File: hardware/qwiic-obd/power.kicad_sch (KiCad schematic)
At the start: 34 parts, among them Q501 DMG2301L, Q502 DMG2301L, Q503 MMBT3906, Q504 DMG2301L, U501 AP63203WU, U502 XC9142B50CMR-G

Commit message: Added initial layout (parts dump)
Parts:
- C508, C509, C512, C513, C514: footprint (none) -> Capacitor_SMD:C_0805_2012Metric_Pad1.18x1.45mm_HandSolder
- L501, L502: footprint (none) -> Inductor_SMD:L_0603_1608Metric_Pad1.05x0.95mm_HandSolder
- U502: footprint SC_50CMR-G_TOR -> UltraLibrarian:XC9142B50CMR-G
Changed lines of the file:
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@@
     (property "Reference" "L502" (id 0) (at 77.47 171.45 90))
     (property "Value" "4.7uH > 1A" (id 1) (at 77.47 173.99 90))
-    (property "Footprint" "" (id 2) (at 77.47 177.8 0)
+    (property "Footprint" "Inductor_SMD:L_0603_1608Metric_Pad1.05x0.95mm_HandSolder" (id 2) (at 77.47 177.8 0)
       (effects (font (size 1.27 1.27)) hide)
     )
@@
     (property "Reference" "L501" (id 0) (at 111.76 102.87 90))
     (property "Value" "3.9uH > 3A" (id 1) (at 111.76 105.41 90))
-    (property "Footprint" "" (id 2) (at 111.76 109.22 0)
+    (property "Footprint" "Inductor_SMD:L_0603_1608Metric_Pad1.05x0.95mm_HandSolder" (id 2) (at 111.76 109.22 0)
       (effects (font (size 1.27 1.27)) hide)
     )
@@
       (effects (font (size 1.27 1.27)) (justify right))
     )
-    (property "Footprint" "" (id 2) (at 115.2652 166.37 0)
+    (property "Footprint" "Capacitor_SMD:C_0805_2012Metric_Pad1.18x1.45mm_HandSolder" (id 2) (at 115.2652 166.37 0)
       (effects (font (size 1.27 1.27)) hide)
     )
@@
       (effects (font (size 1.524 1.524)))
     )
-    (property "Footprint" "SC_50CMR-G_TOR" (id 2) (at 77.47 150.114 0)
+    (property "Footprint" "UltraLibrarian:XC9142B50CMR-G" (id 2) (at 77.47 150.114 0)
       (effects (font (size 1.524 1.524)) hide)
     )
@@
       (effects (font (size 1.27 1.27)) (justify left))
     )
-    (property "Footprint" "" (id 2) (at 60.6552 128.27 0)
+    (property "Footprint" "Capacitor_SMD:C_0805_2012Metric_Pad1.18x1.45mm_HandSolder" (id 2) (at 60.6552 128.27 0)
       (effects (font (size 1.27 1.27)) hide)
     )
@@
       (effects (font (size 1.27 1.27)) (justify left))
     )
-    (property "Footprint" "" (id 2) (at 126.6952 118.11 0)
+    (property "Footprint" "Capacitor_SMD:C_0805_2012Metric_Pad1.18x1.45mm_HandSolder" (id 2) (at 126.6952 118.11 0)
       (effects (font (size 1.27 1.27)) hide)
     )
@@
       (effects (font (size 1.27 1.27)) (justify left))
     )
-    (property "Footprint" "" (id 2) (at 144.4752 118.11 0)
+    (property "Footprint" "Capacitor_SMD:C_0805_2012Metric_Pad1.18x1.45mm_HandSolder" (id 2) (at 144.4752 118.11 0)
       (effects (font (size 1.27 1.27)) hide)
     )
@@
       (effects (font (size 1.27 1.27)) (justify right))
     )
-    (property "Footprint" "" (id 2) (at 46.6852 163.83 0)
-      (effects (font (size 1.27 1.27)) hide)
-    )
+    (property "Footprint" "Capacitor_SMD:C_0805_2012Metric_Pad1.18x1.45mm_HandSolder" (id 2) (at 46.6852 163.83 0)
+      (effects (font (size 1.27 1.27)) hide)
+    )

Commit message: OK, layout v1 complete
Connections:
- net +3V3: no longer C514.2, C515.1, C516.1, R506.1, U502.4 (VOUT)
- new net +5V: C514.2, C515.1, C516.1, R506.1, U502.4 (VOUT)
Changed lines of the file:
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@@
   (junction (at 97.79 49.53) (diameter 0) (color 0 0 0 0)
   )
+  (junction (at 156.21 161.3913) (diameter 0) (color 0 0 0 0)
+  )
   (junction (at 121.92 161.29) (diameter 0) (color 0 0 0 0)
   )
@@
   (junction (at 231.14 49.53) (diameter 0) (color 0 0 0 0)
   )
+  (junction (at 156.21 161.3555) (diameter 0) (color 0 0 0 0)
+  )
   (junction (at 62.23 61.722) (diameter 0) (color 0 0 0 0)
   )
@@
     (stroke (width 0) (type default) (color 0 0 0 0))
   )
+  (wire (pts (xy 165.1 161.3555) (xy 156.21 161.3555))
+    (stroke (width 0) (type default) (color 0 0 0 0))
+  )
   (wire (pts (xy 241.3 44.45) (xy 241.3 49.53))
     (stroke (width 0) (type default) (color 0 0 0 0))
@@
     (stroke (width 0) (type default) (color 0 0 0 0))
   )
-  (wire (pts (xy 156.21 161.29) (xy 166.37 161.29))
-    (stroke (width 0) (type default) (color 0 0 0 0))
-  )
   (wire (pts (xy 185.42 109.22) (xy 193.04 109.22))
     (stroke (width 0) (type default) (color 0 0 0 0))
@@
     (stroke (width 0) (type default) (color 0 0 0 0))
   )
-  (wire (pts (xy 166.37 156.21) (xy 166.37 161.29))
-    (stroke (width 0) (type default) (color 0 0 0 0))
-  )
   (wire (pts (xy 128.27 59.182) (xy 128.27 60.706))
     (stroke (width 0) (type default) (color 0 0 0 0))
@@
     (stroke (width 0) (type default) (color 0 0 0 0))
   )
+  (wire (pts (xy 165.1 154.94) (xy 165.1 161.3555))
+    (stroke (width 0) (type default) (color 0 0 0 0))
+  )
   (wire (pts (xy 62.23 49.53) (xy 62.23 52.324))
     (stroke (width 0) (type default) (color 0 0 0 0))
@@
     (stroke (width 0) (type default) (color 0 0 0 0))
   )
+  (wire (pts (xy 156.21 161.3555) (xy 156.21 161.3913))
+    (stroke (width 0) (type default) (color 0 0 0 0))
+  )
   (wire (pts (xy 45.72 161.29) (xy 45.72 163.83))
     (stroke (width 0) (type default) (color 0 0 0 0))
@@
     (stroke (width 0) (type default) (color 0 0 0 0))
   )
-  (wire (pts (xy 156.21 161.29) (xy 156.21 168.656))
+  (wire (pts (xy 156.21 161.29) (xy 156.21 161.3555))
     (stroke (width 0) (type default) (color 0 0 0 0))
   )
@@
   )
   (wire (pts (xy 52.07 166.37) (xy 52.07 158.75))
+    (stroke (width 0) (type default) (color 0 0 0 0))
+  )
+  (wire (pts (xy 156.21 161.3913) (xy 156.21 168.656))
     (stroke (width 0) (type default) (color 0 0 0 0))
   )
@@
     (pin "2")
   )
+  (symbol (lib_id "power:+5V") (at 165.1 154.94 0) (unit 1)
+    (in_bom yes) (on_board yes) (fields_autoplaced)
+    (property "Reference" "#PWR0520" (id 0) (at 165.1 158.75 0)
+      (effects (font (size 1.27 1.27)) hide)
+    )
+    (property "Value" "+5V" (id 1) (at 165.1 149.86 0))
+    (property "Footprint" "" (id 2) (at 165.1 154.94 0)
+      (effects (font (size 1.27 1.27)) hide)
+    )
+    (property "Datasheet" "" (id 3) (at 165.1 154.94 0)
+      (effects (font (size 1.27 1.27)) hide)
+    )
+    (pin "1")
+  )
   (symbol (lib_id "Transistor_FET:DMG2301L") (at 184.15 52.07 270) (mirror x) (unit 1)
     (in_bom yes) (on_board yes)
@@
     (pin "2")
   )
-  (symbol (lib_id "power:+3V3") (at 166.37 156.21 0) (unit 1)
-    (in_bom yes) (on_board yes) (fields_autoplaced)
-    (property "Reference" "#PWR0520" (id 0) (at 166.37 160.02 0)
-      (effects (font (size 1.27 1.27)) hide)
-    )
-    (property "Value" "+3V3" (id 1) (at 166.37 151.13 0))
-    (property "Footprint" "" (id 2) (at 166.37 156.21 0)
-      (effects (font (size 1.27 1.27)) hide)
-    )
-    (property "Datasheet" "" (id 3) (at 166.37 156.21 0)
-      (effects (font (size 1.27 1.27)) hide)
-    )
-    (pin "1")
-  )
   (symbol (lib_id "Device:C") (at 143.51 114.3 0) (unit 1)

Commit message: Fix title block
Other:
- title: Vehicle CAN Collector -> QWIIC OBDII Interface
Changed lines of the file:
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@@
   (paper "A4")
   (title_block
-    (title "Vehicle CAN Collector")
-    (date "2022-12-29")
+    (title "QWIIC OBDII Interface")
+    (date "2023-01-03")
     (rev "1")
     (company "Gavin Hurlbut")

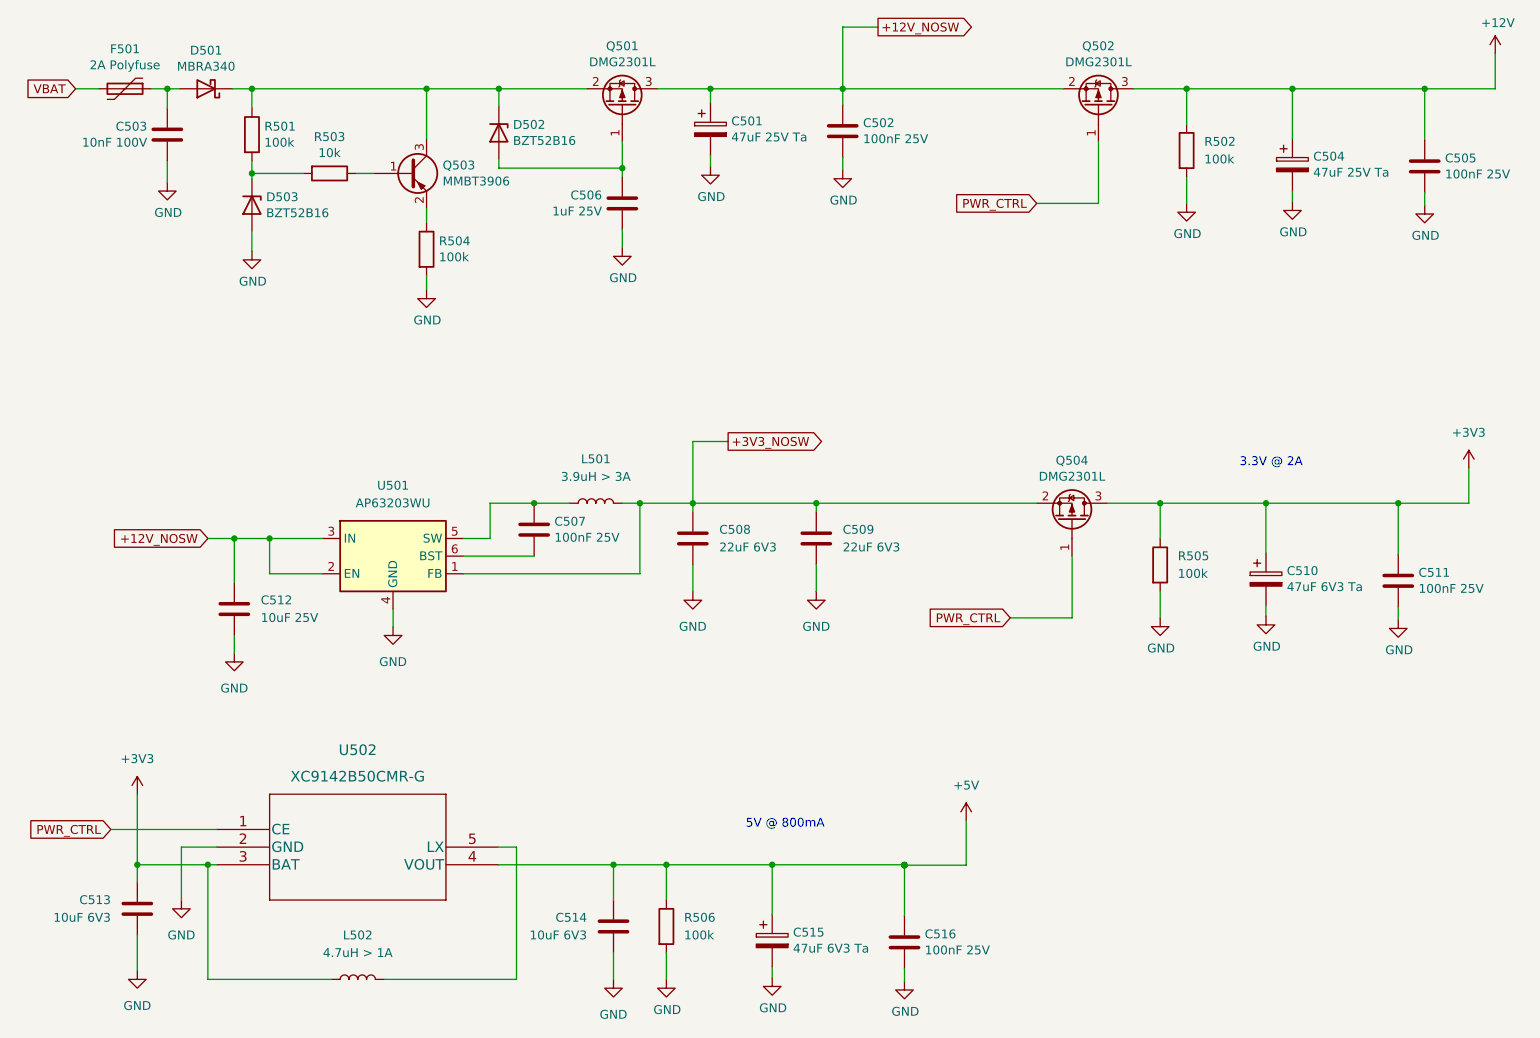
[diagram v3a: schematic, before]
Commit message: Switch out the PIC for an ATtiny424.
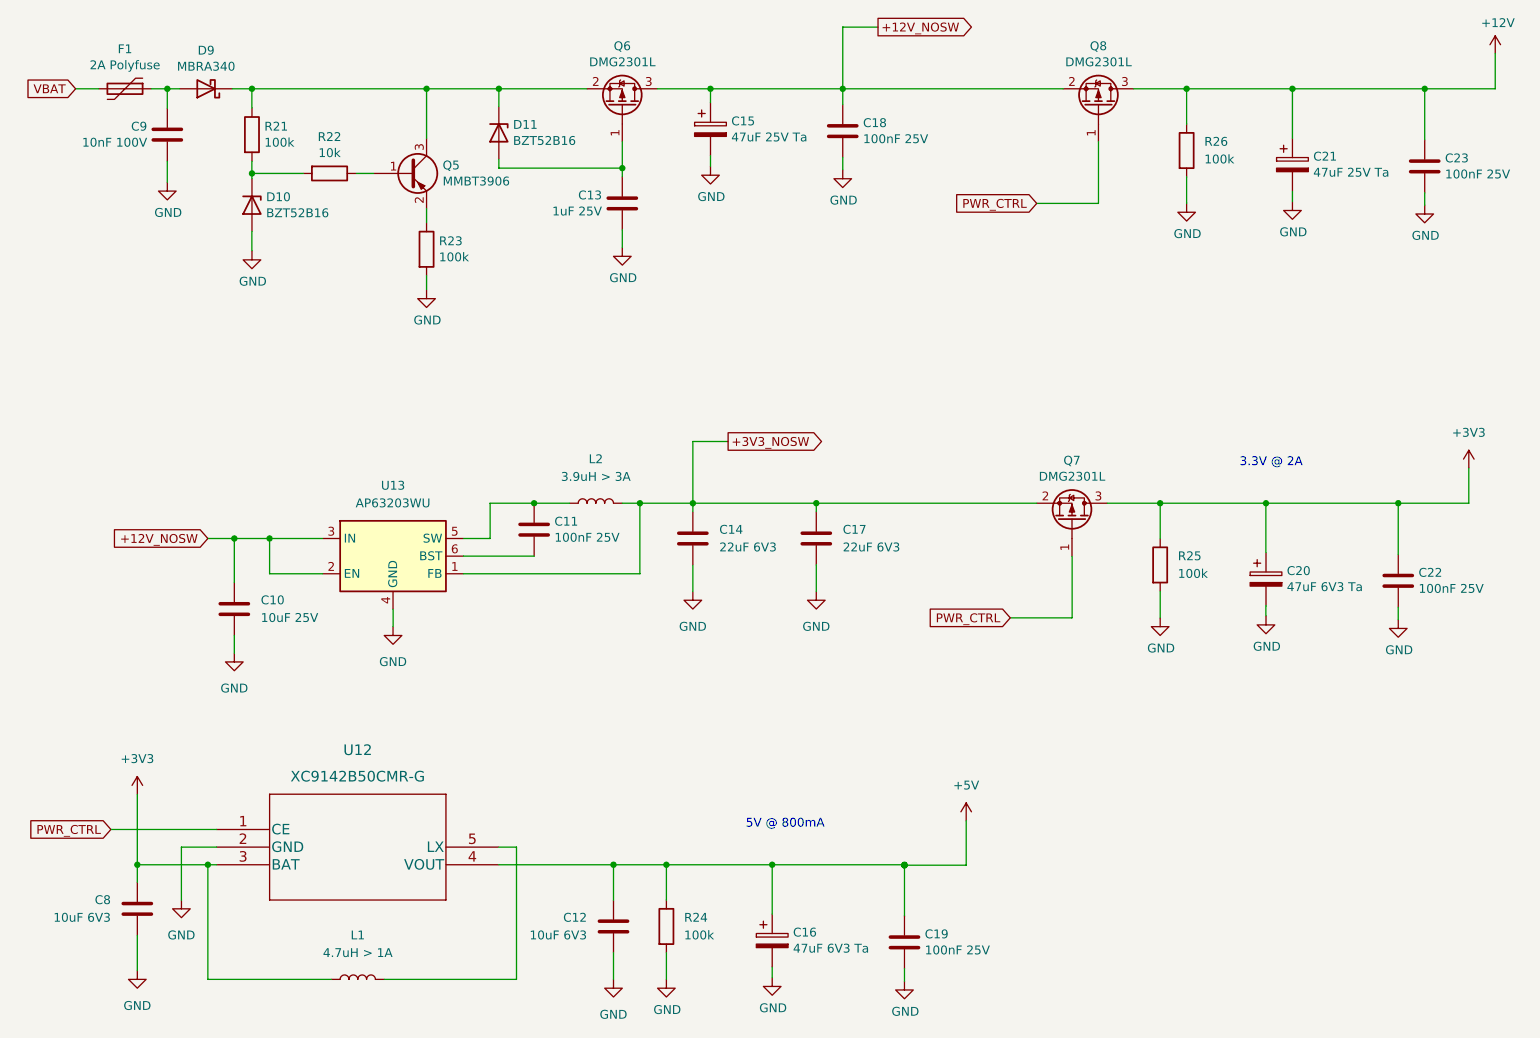
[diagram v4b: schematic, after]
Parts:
- renumbered C512 to C10, C507 to C11, C514 to C12, C506 to C13, C508 to C14, C501 to C15, C515 to C16, C509 to C17, C502 to C18, C516 to C19, C510 to C20, C504 to C21, C511 to C22, C505 to C23, C513 to C8, C503 to C9, D503 to D10, D502 to D11, D501 to D9, F501 to F1, L502 to L1, L501 to L2, Q503 to Q5, Q501 to Q6, Q504 to Q7, Q502 to Q8, R501 to R21, R503 to R22, R504 to R23, R506 to R24, R505 to R25, R502 to R26, U502 to U12, U501 to U13
